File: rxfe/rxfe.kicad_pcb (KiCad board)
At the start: 2 copper layers, 129.3 x 45.7 mm, 82 parts, among them J1 SMA, J2 SMA, J3 4610X-AP1-103LF, J4 SMA, K1 CONN_3, P1 CONN_8X2, U1 SKY12347, U10 SMP1330-005LF, U11 LTC1983-5, U12 SMP1330-005LF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

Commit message: DFM changes to boards - added fiducial markers and increase paste clearance
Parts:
- added FID1: FIDUCIAL, sdtransmitter:FID_1MM, F.Cu at (99.8, 112.3)
- added FID2: FIDUCIAL, sdtransmitter:FID_1MM, F.Cu at (209.3, 125.2)
- added FID3: FIDUCIAL, sdtransmitter:FID_1MM, F.Cu at (206.5, 87.6)
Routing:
- net /T/R: track 93.4 -> 88.2 mm
- net VCC: track 190.9 -> 190.1 mm

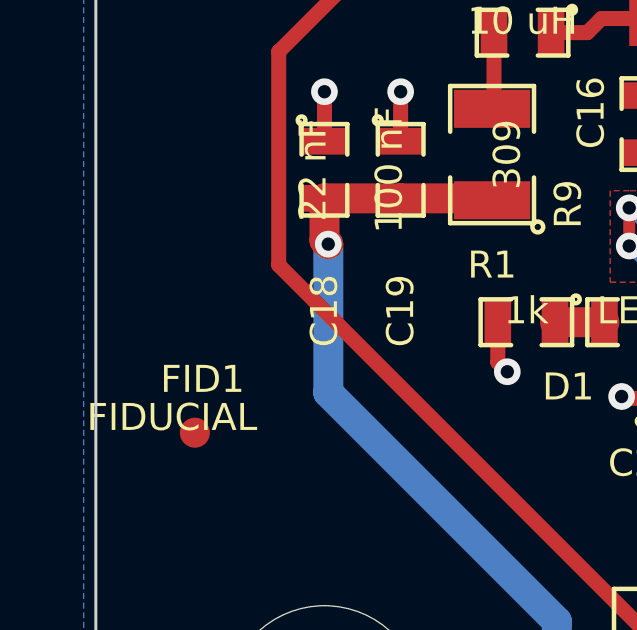
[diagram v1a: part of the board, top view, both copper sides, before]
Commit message: finished layout of DFM'ed driver ampifier board.. except still need to change connectors
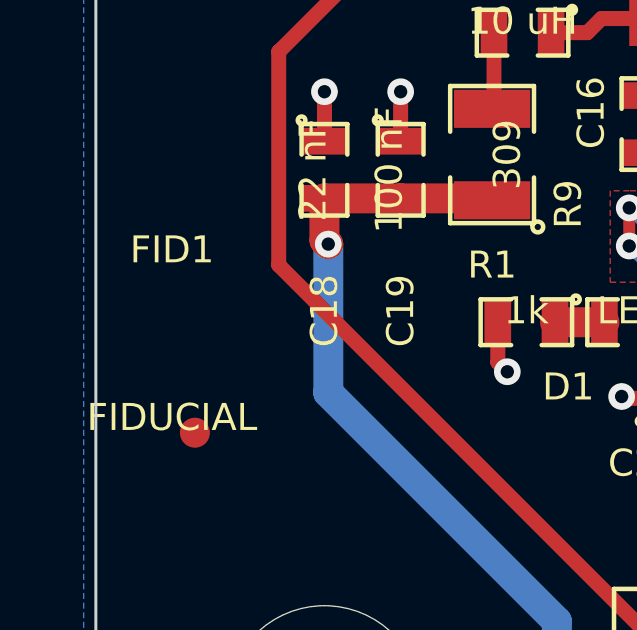
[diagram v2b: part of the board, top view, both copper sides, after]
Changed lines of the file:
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@@
     (links 199)
     (no_connects 0)
-    (area 96.469999 82.499999 225.856001 128.320001)
+    (area 95.836786 78.8416 229.031801 131.267201)
     (thickness 1.6)
     (drawings 20)
@@
   )
   (setup
-    (last_trace_width 0.5)
+    (last_trace_width 0.254)
     (user_trace_width 0.25)
     (user_trace_width 0.4)
@@
   (module sdtransmitter:FID_1MM (layer F.Cu)
     (at 99.822 112.268)
-    (fp_text reference FID1 (at 0.254 -1.778) (layer F.SilkS)
+    (fp_text reference FID1 (at -0.762 -6.096) (layer F.SilkS)
       (effects (font (size 0.9 0.9) (thickness 0.175)))
     )
@@
   (segment (start 147.828 87.249) (end 141.6685 87.249) (width 0.5) (layer F.Cu) (net 56))
   (segment (start 107.188 97.0534) (end 105.1306 97.0534) (width 0.5) (layer F.Cu) (net 57))
-  (segment (start 115.316 119.38) (end 116.332 119.38) (width 0.5) (layer F.Cu) (net 57) (status 800000))
+  (segment (start 115.316 119.38) (end 116.332 119.38) (width 0.5) (layer F.Cu) (net 57))
   (segment (start 102.616 106.68) (end 115.316 119.38) (width 0.5) (layer F.Cu) (net 57))
   (segment (start 102.616 99.568) (end 102.616 106.68) (width 0.5) (layer F.Cu) (net 57))

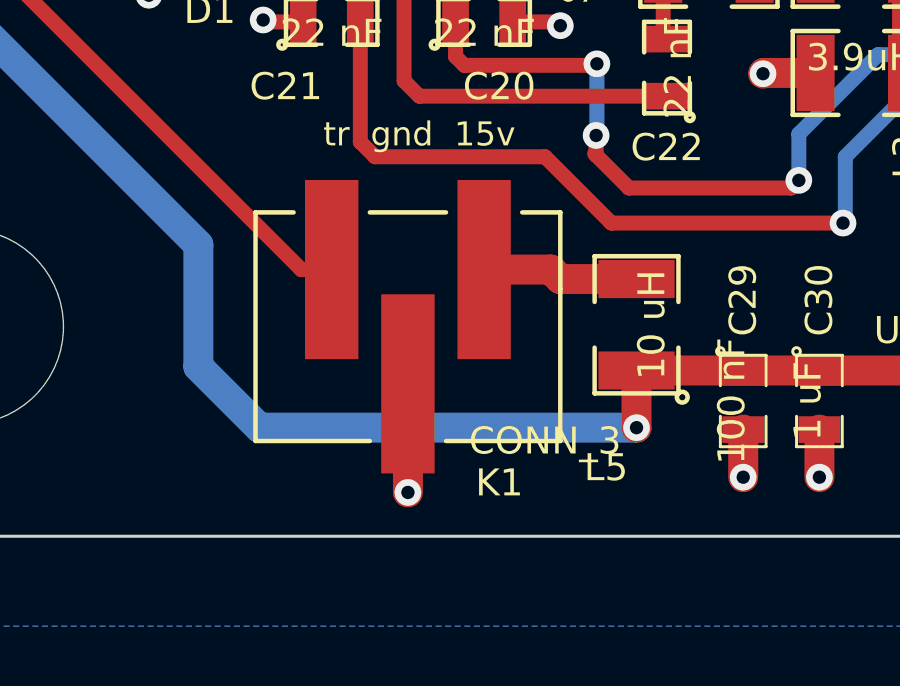
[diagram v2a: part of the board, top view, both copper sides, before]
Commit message: changed all 3 pin headers to molex smd connectors available in tube packaging..
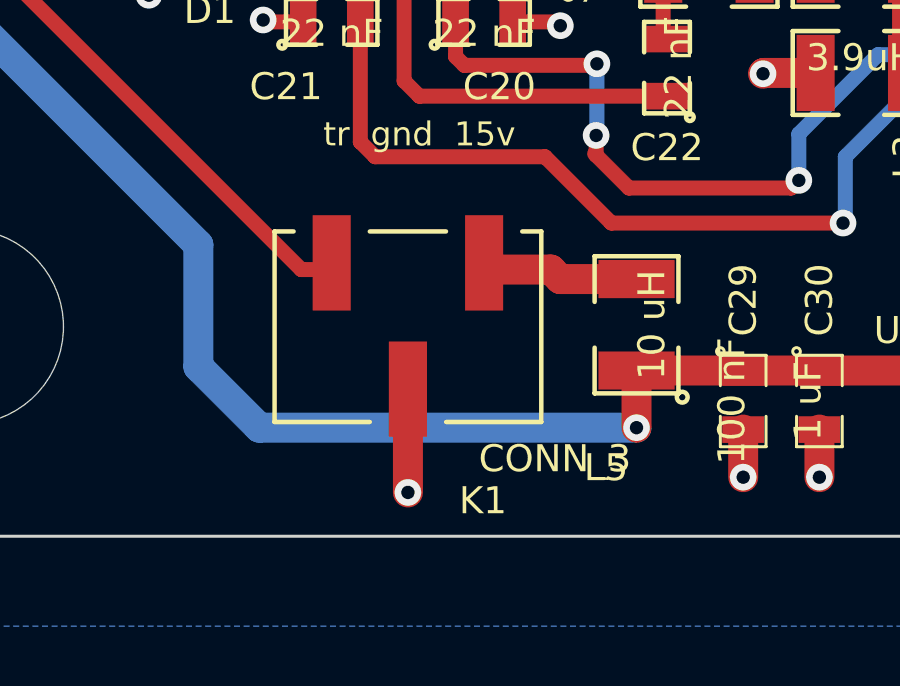
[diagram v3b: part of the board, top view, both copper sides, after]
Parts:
- K1: footprint localconn:3-647166-3 -> sdtransmitter:0740991003

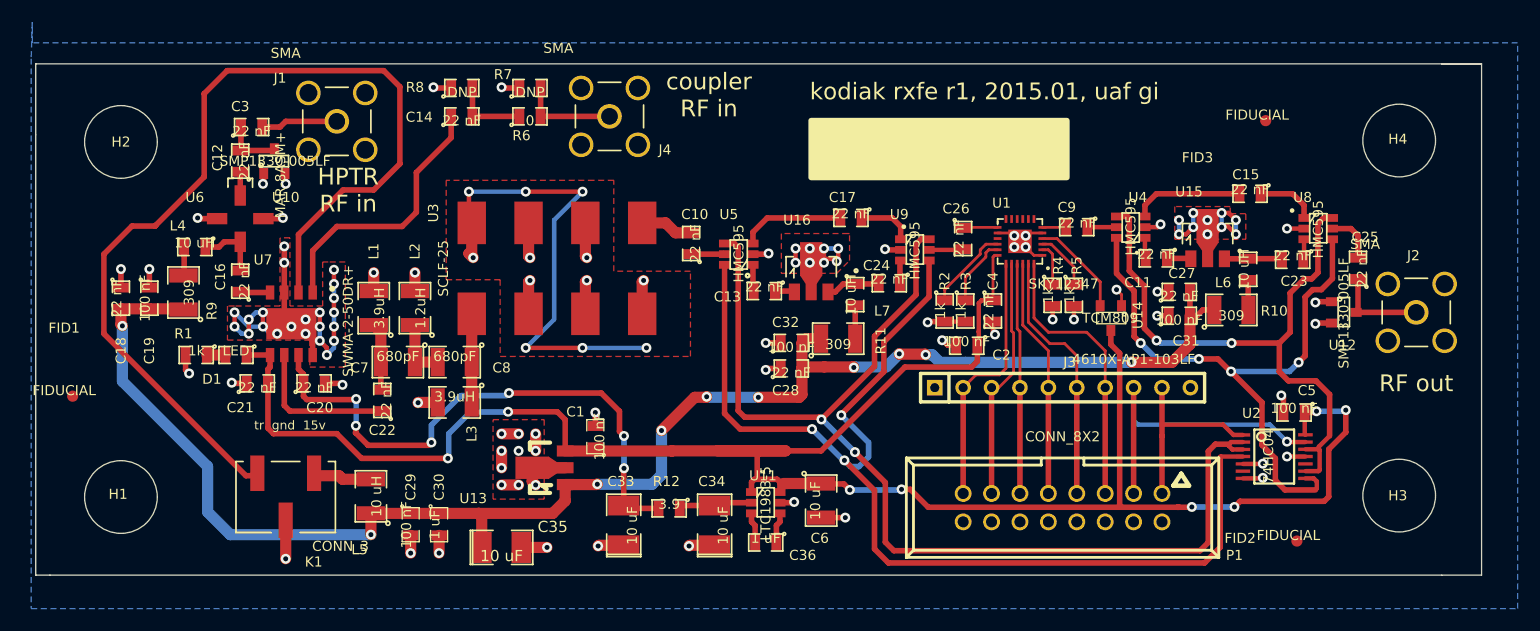
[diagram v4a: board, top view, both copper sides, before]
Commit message: cleaned up silkscreen, moved fiduciary marks at least 4.75ish mm away from board edges
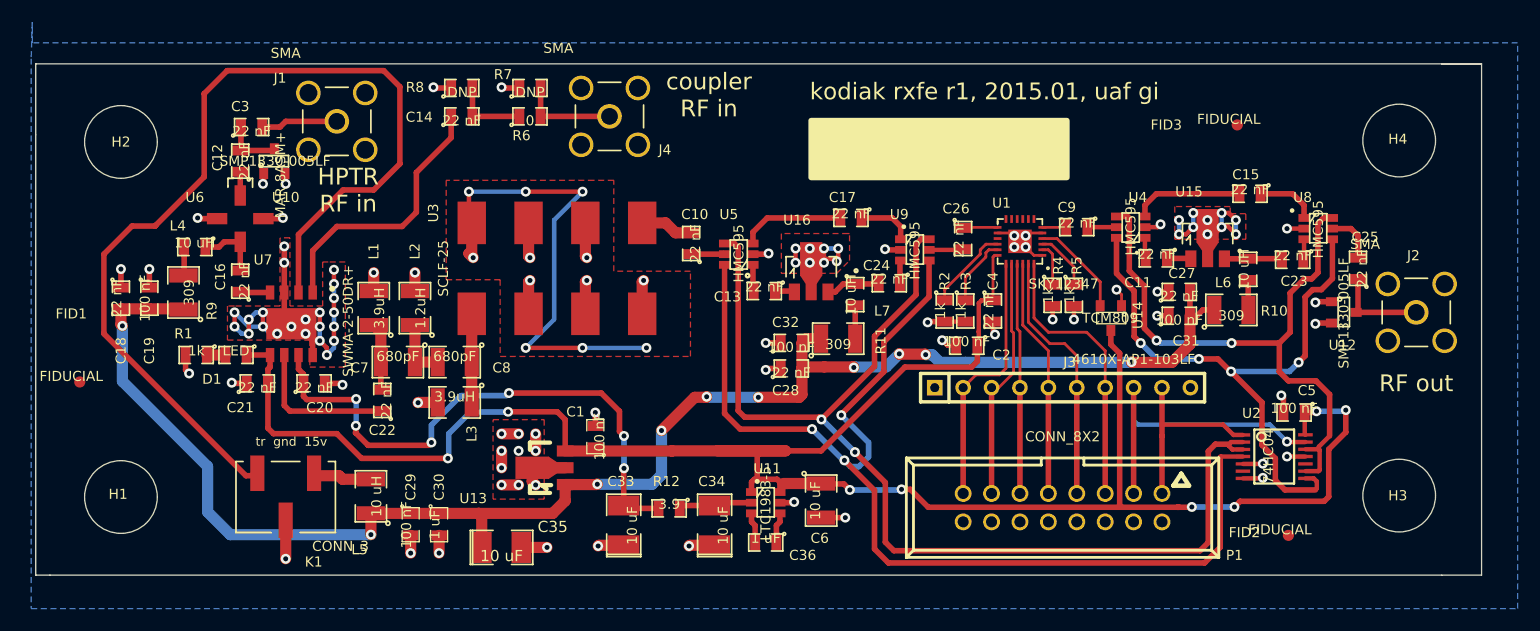
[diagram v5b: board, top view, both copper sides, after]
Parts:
- moved FID3 2.57 mm to (204.0, 88.0)
- moved FID1 1.42 mm to (100.5, 111.0)
- moved FID2 0.92 mm to (208.5, 124.7)
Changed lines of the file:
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@@
     (area 95.836786 78.8416 229.031801 131.267201)
     (thickness 1.6)
-    (drawings 20)
+    (drawings 21)
     (tracks 811)
     (zones 0)
@@
   )
   (setup
-    (last_trace_width 0.254)
+    (last_trace_width 0.4)
     (user_trace_width 0.25)
     (user_trace_width 0.4)
@@
     (visible_elements FFFEFF7F)
     (pcbplotparams
-      (layerselection 284196865)
+      (layerselection 284721153)
       (usegerberextensions true)
       (excludeedgelayer true)
@@
   (module SMD_Packages:SOT-23-6 (layer F.Cu)
     (at 161.798 121.793 270)
-    (fp_text reference U11 (at -2.413 0.254 360) (layer F.SilkS)
+    (fp_text reference U11 (at -3.048 -0.127 360) (layer F.SilkS)
       (effects (font (size 0.9 0.9) (thickness 0.2)))
     )
@@
   )
   (module sdtransmitter:FID_1MM (layer F.Cu)
-    (at 99.822 112.268)
+    (at 100.457 110.998)
     (fp_text reference FID1 (at -0.762 -6.096) (layer F.SilkS)
       (effects (font (size 0.9 0.9) (thickness 0.175)))
@@
   )
   (module sdtransmitter:FID_1MM (layer F.Cu)
-    (at 209.296 125.222)
-    (fp_text reference FID2 (at -5.08 -0.254) (layer F.SilkS)
+    (at 208.534 124.714)
+    (fp_text reference FID2 (at -3.937 -0.254) (layer F.SilkS)
       (effects (font (size 0.9 0.9) (thickness 0.175)))
     )
@@
   )
   (module sdtransmitter:FID_1MM (layer F.Cu)
-    (at 206.502 87.63)
-    (fp_text reference FID3 (at -6.096 3.302) (layer F.SilkS)
+    (at 203.962 88.011)
+    (fp_text reference FID3 (at -6.35 0) (layer F.SilkS)
       (effects (font (size 0.9 0.9) (thickness 0.175)))
     )
@@
       (net 57 /T/R))
   )
+  (gr_circle (center 161.036 119.888) (end 161.163 119.888) (layer F.SilkS) (width 0.2))
   (gr_text "RF out" (at 219.964 111.125) (layer F.SilkS)
     (effects (font (size 1.5 1.5) (thickness 0.3)))
@@
   (gr_line (start 96.52 82.55) (end 222.25 82.55) (angle 90) (layer Edge.Cuts) (width 0.1))
   (gr_line (start 96.52 88.9) (end 96.52 82.55) (angle 90) (layer Edge.Cuts) (width 0.1))
-  (gr_text "tr  gnd  15v" (at 119.253 114.8715) (layer F.SilkS)
+  (gr_text "tr  gnd  15v" (at 119.38 116.332) (layer F.SilkS)
     (effects (font (size 0.8 0.8) (thickness 0.2)))
   )

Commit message: DFM changes..
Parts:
- removed R7: 0, SMD_Packages:SMD-0805
- added C37: 22 nF, SMD_Packages:SMD-0805, F.Cu at (140.7, 87.1)
- J1, J2, J4: footprint local:SMA_5-1814832-1 -> local:SMA_0732511350
- moved FID1 1.78 mm to (102.2, 111.1)
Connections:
- net VCC renamed +5V
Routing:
- net GND: track 242.7 -> 267.0 mm, vias 109 -> 122
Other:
- board size 129.3 x 45.7 mm -> 129.5 x 46.2 mm

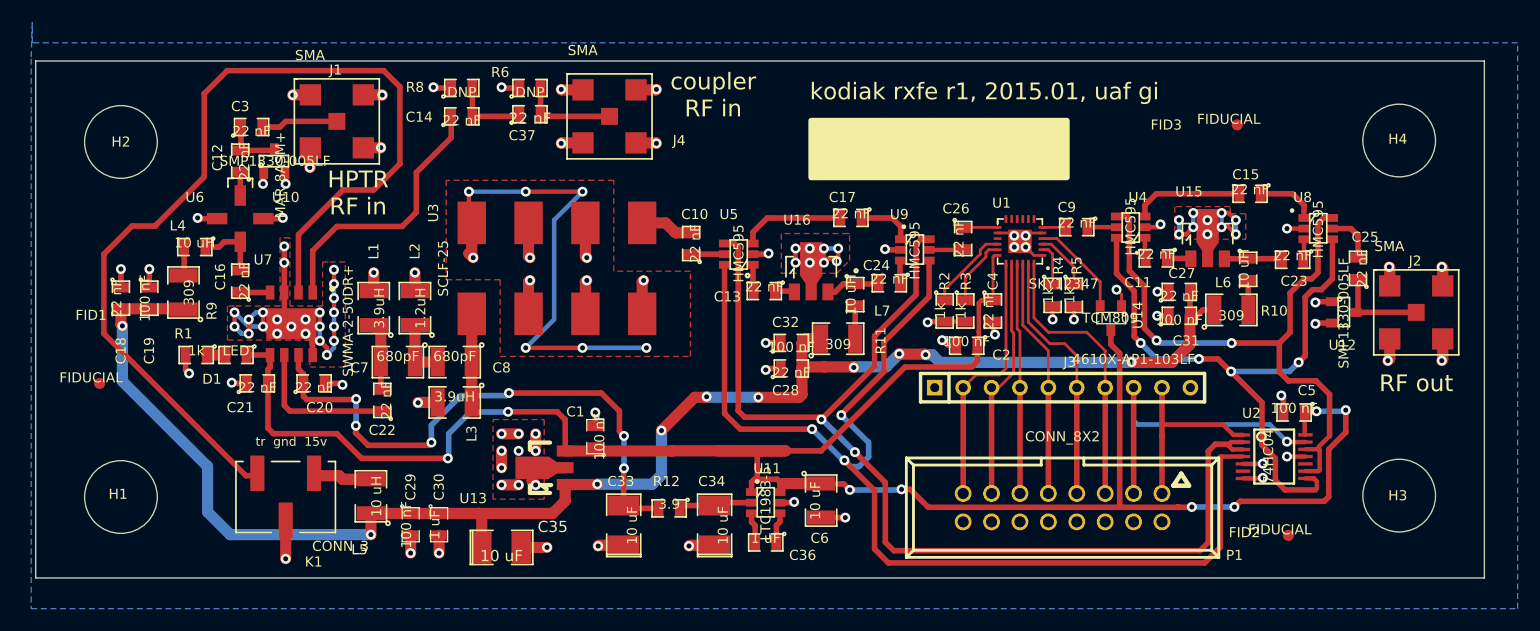
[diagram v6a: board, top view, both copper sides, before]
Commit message: component footprint changes to simplify bom
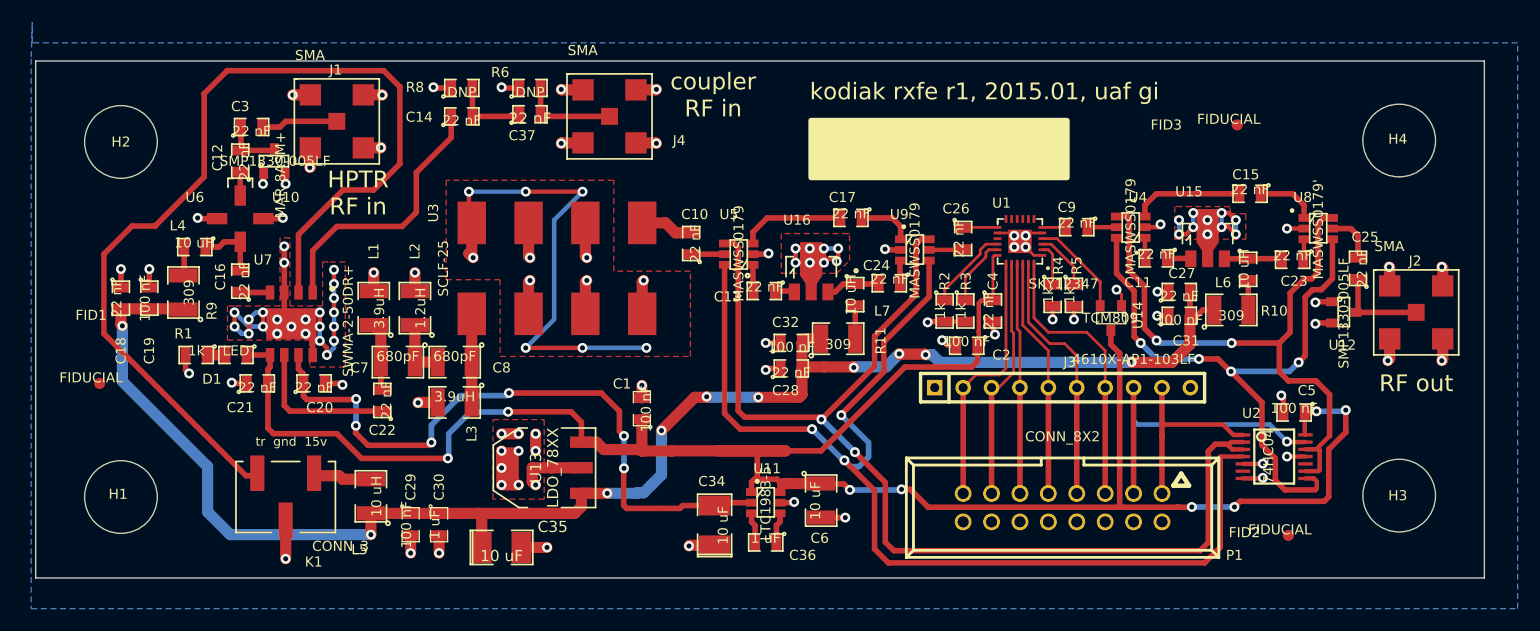
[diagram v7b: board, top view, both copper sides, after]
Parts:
- removed C33: 10 uF, SMD_Packages:SMD-1210_Pol
- removed R12: 3.9, SMD_Packages:SMD-0805
- U13: footprint Housings_SOT-89:SOT89-3_Housing -> SMD_Packages:SOT-223
- U4, U5, U9: value HMC595 -> MASWSS0179
- U8: value HMC595 -> MASWSS0179'
- moved C1 4.86 mm to (150.7, 113.4)
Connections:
- net +5V renamed VCC
- C34 pad 2: Net-(C34-Pad2) -> -5V
- U11 pad 2: Net-(C34-Pad2) -> -5V
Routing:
- net -5V: track 51.2 -> 59.8 mm
- net Net-(C34-Pad2): track 6.62 -> 0.00 mm
- net GND: track 267.0 -> 264.4 mm, vias 122 -> 121
- net VCC: track 190.1 -> 191.7 mm

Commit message: added scripts for using gerbmerge for panelizing boards to reduce assembly costs
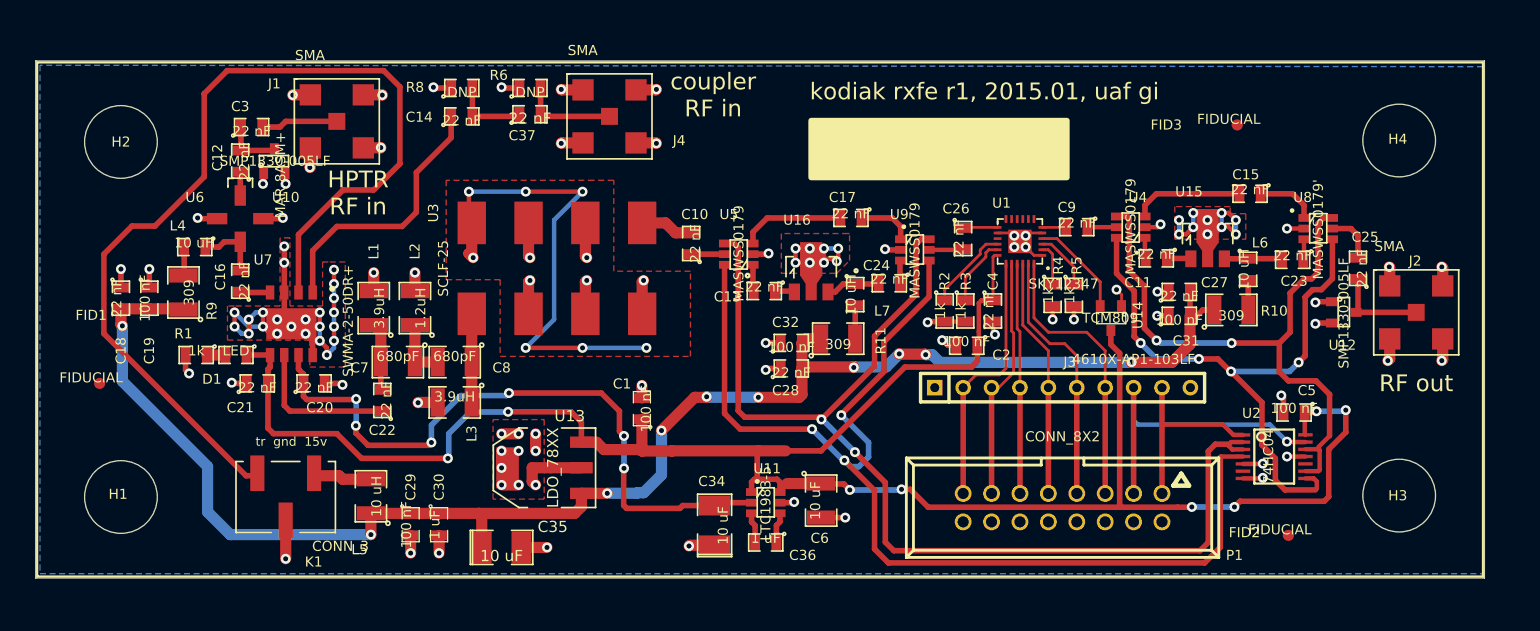
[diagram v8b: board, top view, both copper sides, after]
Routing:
- net VCC: track 191.7 -> 184.4 mm
- net VDD: track 150.6 -> 150.0 mm
